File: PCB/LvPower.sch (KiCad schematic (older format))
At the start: 0 parts

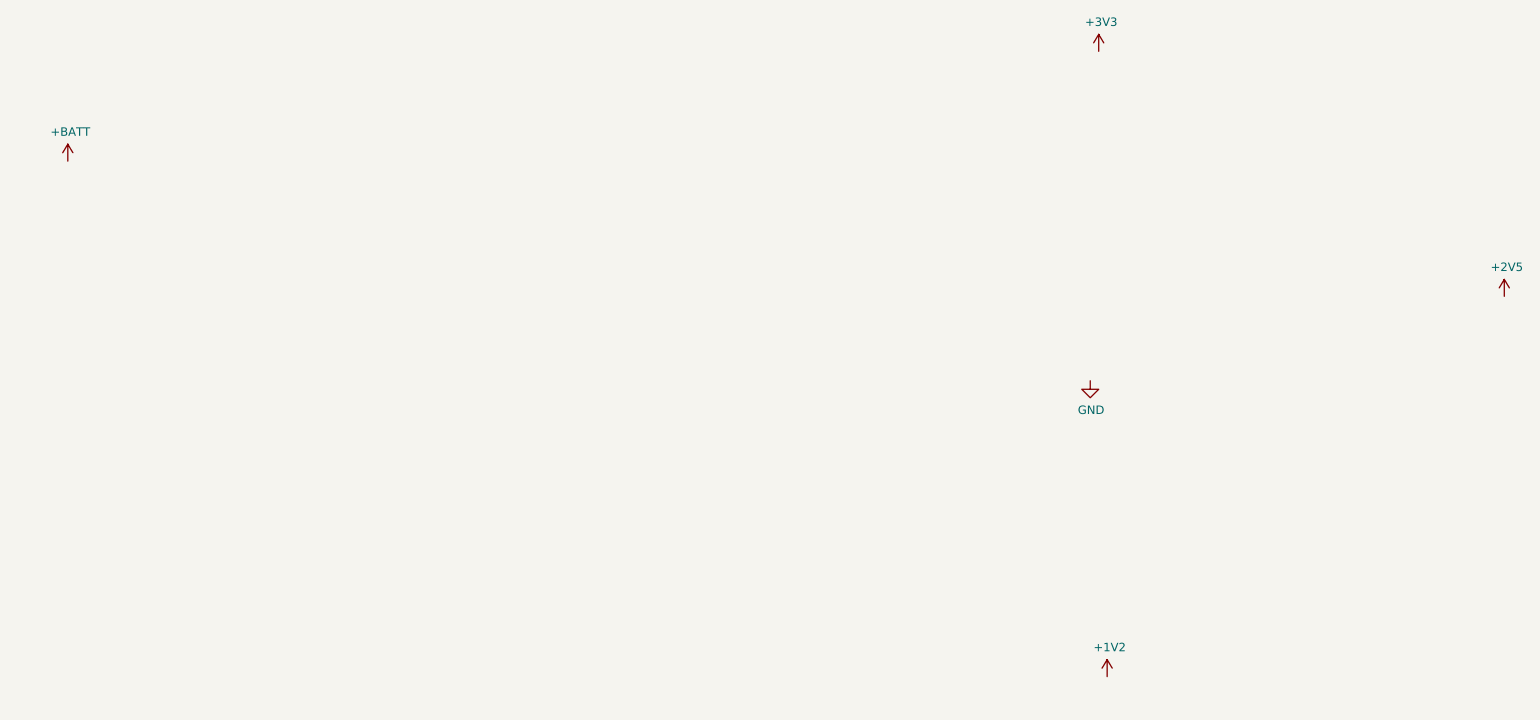
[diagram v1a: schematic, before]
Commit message: Cleanup FPGA ground pins in library, begin adding components to schematic
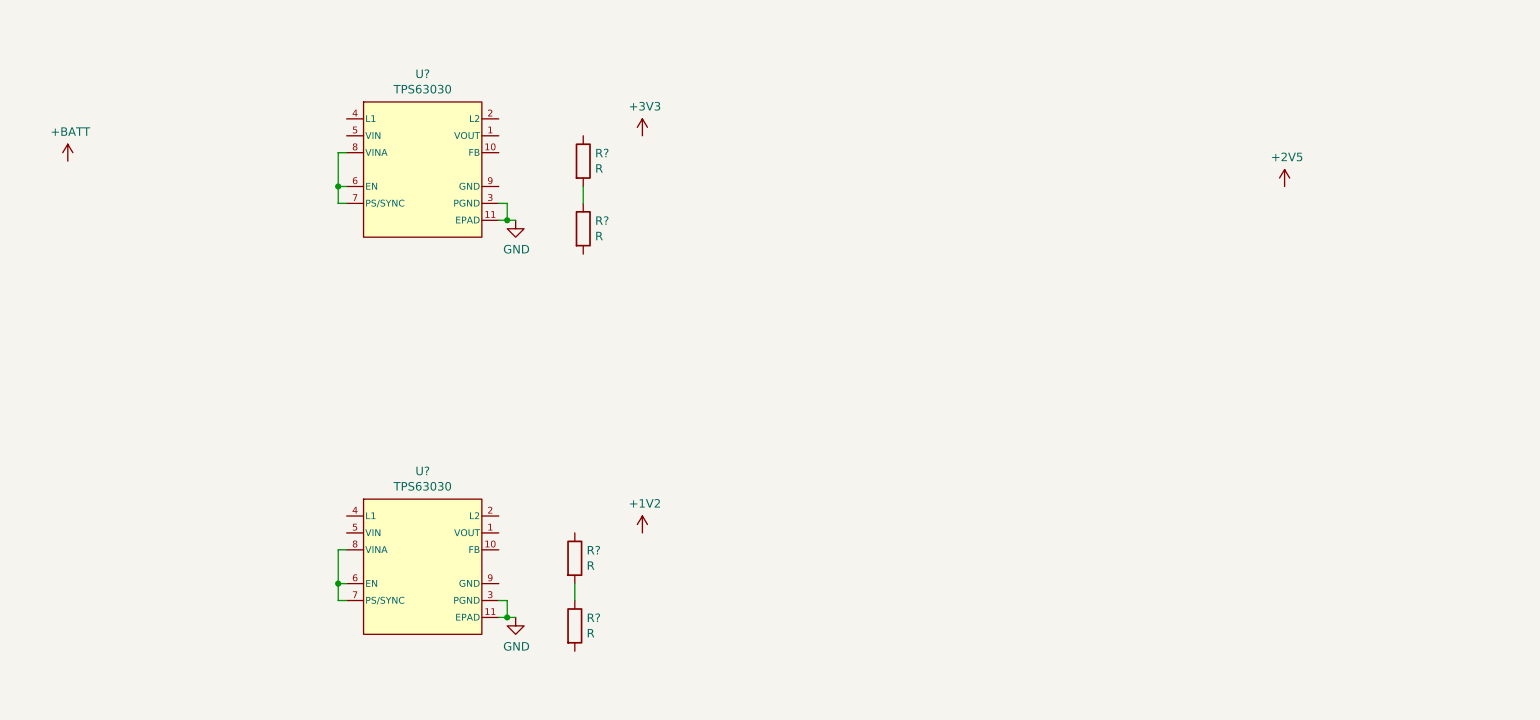
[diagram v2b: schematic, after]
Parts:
- added R? (x4): R, symbol Device:R
- added U? (x2): TPS63030, Parts:WSON10-PAD, symbol Parts:TPS63030
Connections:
- net GND: now also U?.11 (EPAD), U?.11 (EPAD), U?.3 (PGND), U?.3 (PGND)
- new net: U?.6 (EN), U?.7 (PS/SYNC), U?.8 (VINA) (x2)
- new net: R?.1, R?.2 (x2)
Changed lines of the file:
@@
 L power:+3V3 #PWR?
 U 1 1 5DCD8EE2
-P 8050 2000
-F 0 "#PWR?" H 8050 1850 50  0001 C CNN
-F 1 "+3V3" H 8065 2173 50  0000 C CNN
-F 2 "" H 8050 2000 50  0001 C CNN
-F 3 "" H 8050 2000 50  0001 C CNN
-	1    8050 2000
+P 5350 2500
+F 0 "#PWR?" H 5350 2350 50  0001 C CNN
+F 1 "+3V3" H 5365 2673 50  0000 C CNN
+F 2 "" H 5350 2500 50  0001 C CNN
+F 3 "" H 5350 2500 50  0001 C CNN
+	1    5350 2500
 	1    0    0    -1
 $EndComp
@@
 L power:+1V2 #PWR?
 U 1 1 5DCD9F72
-P 8100 5700
-F 0 "#PWR?" H 8100 5550 50  0001 C CNN
-F 1 "+1V2" H 8115 5873 50  0000 C CNN
-F 2 "" H 8100 5700 50  0001 C CNN
-F 3 "" H 8100 5700 50  0001 C CNN
-	1    8100 5700
+P 5350 4850
+F 0 "#PWR?" H 5350 4700 50  0001 C CNN
+F 1 "+1V2" H 5365 5023 50  0000 C CNN
+F 2 "" H 5350 4850 50  0001 C CNN
+F 3 "" H 5350 4850 50  0001 C CNN
+	1    5350 4850
 	1    0    0    -1
 $EndComp
@@
 L power:+2V5 #PWR?
 U 1 1 5DCDA97B
-P 10450 3450
-F 0 "#PWR?" H 10450 3300 50  0001 C CNN
-F 1 "+2V5" H 10465 3623 50  0000 C CNN
-F 2 "" H 10450 3450 50  0001 C CNN
-F 3 "" H 10450 3450 50  0001 C CNN
-	1    10450 3450
+P 9150 2800
+F 0 "#PWR?" H 9150 2650 50  0001 C CNN
+F 1 "+2V5" H 9165 2973 50  0000 C CNN
+F 2 "" H 9150 2800 50  0001 C CNN
+F 3 "" H 9150 2800 50  0001 C CNN
+	1    9150 2800
 	1    0    0    -1
 $EndComp
@@
 L power:GND #PWR?
 U 1 1 5DCDBC9C
-P 8000 3950
-F 0 "#PWR?" H 8000 3700 50  0001 C CNN
-F 1 "GND" H 8005 3777 50  0000 C CNN
-F 2 "" H 8000 3950 50  0001 C CNN
-F 3 "" H 8000 3950 50  0001 C CNN
-	1    8000 3950
+P 4600 3000
+F 0 "#PWR?" H 4600 2750 50  0001 C CNN
+F 1 "GND" H 4605 2827 50  0000 C CNN
+F 2 "" H 4600 3000 50  0001 C CNN
+F 3 "" H 4600 3000 50  0001 C CNN
+	1    4600 3000
 	1    0    0    -1
 $EndComp
+$Comp
+L Parts:TPS63030 U?
+U 1 1 5DCF7F00
+P 4050 2700
+F 0 "U?" H 4050 3265 50  0000 C CNN
+F 1 "TPS63030" H 4050 3174 50  0000 C CNN
+F 2 "Parts:WSON10-PAD" H 4050 2250 60  0001 C CNN
+F 3 "http://www.ti.com/product/TPS63030" H 3600 2600 60  0001 C CNN
+	1    4050 2700
+	1    0    0    -1
+$EndComp
+$Comp
+L Parts:TPS63030 U?
+U 1 1 5DCF8885
+P 4050 5050
+F 0 "U?" H 4050 5615 50  0000 C CNN
+F 1 "TPS63030" H 4050 5524 50  0000 C CNN
+F 2 "Parts:WSON10-PAD" H 4050 4600 60  0001 C CNN
+F 3 "http://www.ti.com/product/TPS63030" H 3600 4950 60  0001 C CNN
+	1    4050 5050
+	1    0    0    -1
+$EndComp
+$Comp
+L power:GND #PWR?
+U 1 1 5DCF9CED
+P 4600 5350
+F 0 "#PWR?" H 4600 5100 50  0001 C CNN
+F 1 "GND" H 4605 5177 50  0000 C CNN
+F 2 "" H 4600 5350 50  0001 C CNN
+F 3 "" H 4600 5350 50  0001 C CNN
+	1    4600 5350
+	1    0    0    -1
+$EndComp
+Wire Wire Line
+	4600 5350 4550 5350
+Wire Wire Line
+	4500 3000 4550 3000
+Wire Wire Line
+	4500 2900 4550 2900
+Wire Wire Line
+	4550 2900 4550 3000
+Connection ~ 4550 3000
+Wire Wire Line
+	4550 3000 4600 3000
+Wire Wire Line
+	4500 5250 4550 5250
+Wire Wire Line
+	4550 5250 4550 5350
+Connection ~ 4550 5350
+Wire Wire Line
+	4550 5350 4500 5350
+$Comp
+L Device:R R?
+U 1 1 5DCFD0C2
+P 5000 3050
+F 0 "R?" H 5070 3096 50  0000 L CNN
+F 1 "R" H 5070 3005 50  0000 L CNN
+F 2 "" V 4930 3050 50  0001 C CNN
+F 3 "~" H 5000 3050 50  0001 C CNN
+	1    5000 3050
+	1    0    0    -1
+$EndComp
+$Comp
+L Device:R R?
+U 1 1 5DCFE76B
+P 5000 2650
+F 0 "R?" H 5070 2696 50  0000 L CNN
+F 1 "R" H 5070 2605 50  0000 L CNN
+F 2 "" V 4930 2650 50  0001 C CNN
+F 3 "~" H 5000 2650 50  0001 C CNN
+	1    5000 2650
+	1    0    0    -1
+$EndComp
+Wire Wire Line
+	5000 2800 5000 2900
+$Comp
+L Device:R R?
+U 1 1 5DD00F6F
+P 4950 5000
+F 0 "R?" H 5020 5046 50  0000 L CNN
+F 1 "R" H 5020 4955 50  0000 L CNN
+F 2 "" V 4880 5000 50  0001 C CNN
+F 3 "~" H 4950 5000 50  0001 C CNN
+	1    4950 5000
+	1    0    0    -1
+$EndComp
+$Comp
+L Device:R R?
+U 1 1 5DD0194C
+P 4950 5400
+F 0 "R?" H 5020 5446 50  0000 L CNN
+F 1 "R" H 5020 5355 50  0000 L CNN
+F 2 "" V 4880 5400 50  0001 C CNN
+F 3 "~" H 4950 5400 50  0001 C CNN
+	1    4950 5400
+	1    0    0    -1
+$EndComp
+Wire Wire Line
+	4950 5150 4950 5250
+Wire Wire Line
+	3600 2600 3550 2600
+Wire Wire Line
+	3550 2600 3550 2800
+Wire Wire Line
+	3550 2800 3600 2800
+Wire Wire Line
+	3550 2800 3550 2900
+Wire Wire Line
+	3550 2900 3600 2900
+Connection ~ 3550 2800
+Wire Wire Line
+	3600 4950 3550 4950
+Wire Wire Line
+	3550 4950 3550 5150
+Wire Wire Line
+	3550 5150 3600 5150
+Wire Wire Line
+	3550 5150 3550 5250
+Wire Wire Line
+	3550 5250 3600 5250
+Connection ~ 3550 5150
 $EndSCHEMATC

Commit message: Add linear regulator and JST-PH connector to library
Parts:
- added R? (x2): R, symbol Device:R
- added U?: AP2202K-ADJTRG1, Parts:SOT23-5, symbol Parts:AP2202K-ADJTRG1
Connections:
- wire segments 20 -> 21
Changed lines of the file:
@@
 L power:+2V5 #PWR?
 U 1 1 5DCDA97B
-P 9150 2800
-F 0 "#PWR?" H 9150 2650 50  0001 C CNN
-F 1 "+2V5" H 9165 2973 50  0000 C CNN
-F 2 "" H 9150 2800 50  0001 C CNN
-F 3 "" H 9150 2800 50  0001 C CNN
-	1    9150 2800
+P 9250 2800
+F 0 "#PWR?" H 9250 2650 50  0001 C CNN
+F 1 "+2V5" H 9265 2973 50  0000 C CNN
+F 2 "" H 9250 2800 50  0001 C CNN
+F 3 "" H 9250 2800 50  0001 C CNN
+	1    9250 2800
 	1    0    0    -1
 $EndComp
@@
 L power:+BATT #PWR?
 U 1 1 5DCDADE4
-P 1950 2650
-F 0 "#PWR?" H 1950 2500 50  0001 C CNN
-F 1 "+BATT" H 1965 2823 50  0000 C CNN
-F 2 "" H 1950 2650 50  0001 C CNN
-F 3 "" H 1950 2650 50  0001 C CNN
-	1    1950 2650
+P 1750 2100
+F 0 "#PWR?" H 1750 1950 50  0001 C CNN
+F 1 "+BATT" H 1765 2273 50  0000 C CNN
+F 2 "" H 1750 2100 50  0001 C CNN
+F 3 "" H 1750 2100 50  0001 C CNN
+	1    1750 2100
 	1    0    0    -1
 $EndComp
@@
 	3550 5250 3600 5250
 Connection ~ 3550 5150
+$Comp
+L Device:R R?
+U 1 1 5DCE675A
+P 8950 2950
+F 0 "R?" H 9020 2996 50  0000 L CNN
+F 1 "R" H 9020 2905 50  0000 L CNN
+F 2 "" V 8880 2950 50  0001 C CNN
+F 3 "~" H 8950 2950 50  0001 C CNN
+	1    8950 2950
+	1    0    0    -1
+$EndComp
+$Comp
+L Device:R R?
+U 1 1 5DCE7121
+P 8950 3350
+F 0 "R?" H 9020 3396 50  0000 L CNN
+F 1 "R" H 9020 3305 50  0000 L CNN
+F 2 "" V 8880 3350 50  0001 C CNN
+F 3 "~" H 8950 3350 50  0001 C CNN
+	1    8950 3350
+	1    0    0    -1
+$EndComp
+Wire Wire Line
+	8950 3100 8950 3200
+$Comp
+L Parts:AP2202K-ADJTRG1 U?
+U 1 1 5DCE8C9B
+P 8200 2900
+F 0 "U?" H 8200 3265 50  0000 C CNN
+F 1 "AP2202K-ADJTRG1" H 8200 3174 50  0000 C CNN
+F 2 "Parts:SOT23-5" H 8200 2550 50  0001 C CNN
+F 3 "https://www.diodes.com/part/view/AP2202" H 8200 2550 50  0001 C CNN
+	1    8200 2900
+	1    0    0    -1
+$EndComp
 $EndSCHEMATC

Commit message: Switch to cheaper linear regulator (with better datasheet), finish LvPower schematic
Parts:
- removed R? (x4): R, symbol Device:R
- removed U?: AP2202K-ADJTRG1, Parts:SOT23-5, symbol Parts:AP2202K-ADJTRG1
- removed U?: TPS63030, Parts:WSON10-PAD, symbol Parts:TPS63030
- added C? (x6): 10uF, Capacitors_SMD:C_0805_HandSoldering, symbol Device:C_Small
- added C? (x2): 100nF, Capacitors_SMD:C_0402, symbol Device:C_Small
- added C? (x2): 1uF, Capacitors_SMD:C_0603_HandSoldering, symbol Device:C_Small
- added L? (x2): 1.5uH, Inductors:Inductor_Taiyo-Yuden_MD-3030, symbol Device:L_Core_Ferrite_Small
- added NT? (x2): Net-Tie_2, symbol Device:Net-Tie_2
- added R?: 280k, Resistors_SMD:R_0603_HandSoldering, symbol Device:R
- added R?: 200k, Resistors_SMD:R_0603_HandSoldering, symbol Device:R
- added R?: 120k, Resistors_SMD:R_0805_HandSoldering, symbol Device:R
- added U?: TPS63030, Parts:WSON10-PAD, symbol Parts:TPS63030
- added U?: TCR2EF25, Parts:SOT23-5, symbol Parts:TCR2EF25
- R?: value R -> 200k; footprint (none) -> Resistors_SMD:R_0603_HandSoldering
- R?: value R -> 1M; footprint (none) -> Resistors_SMD:R_0805_HandSoldering
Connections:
- net labels added: GNDA-1V2, GNDA-3V3
- wire segments 21 -> 96
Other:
- moved on the sheet: R?

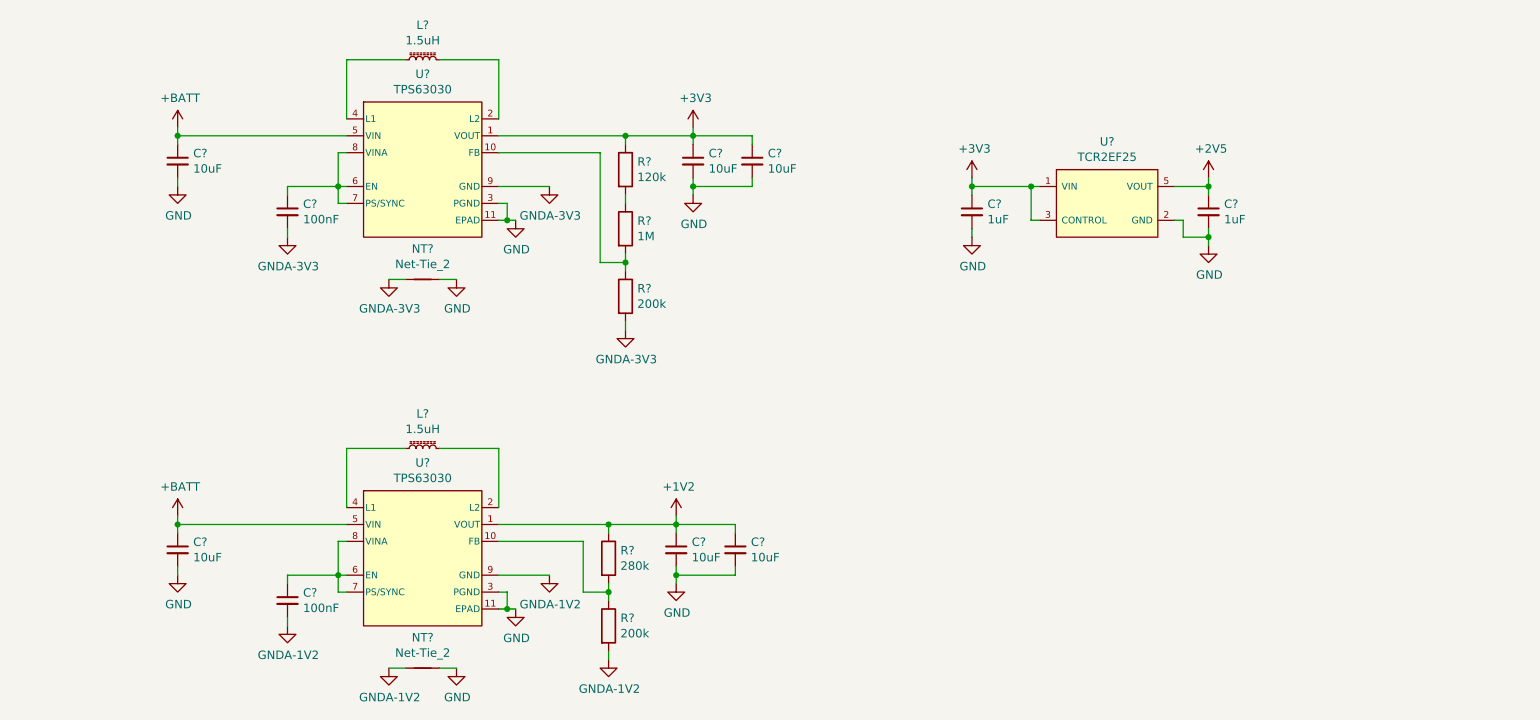
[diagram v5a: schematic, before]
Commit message: Switch 1.2V supply to use new buck regulator
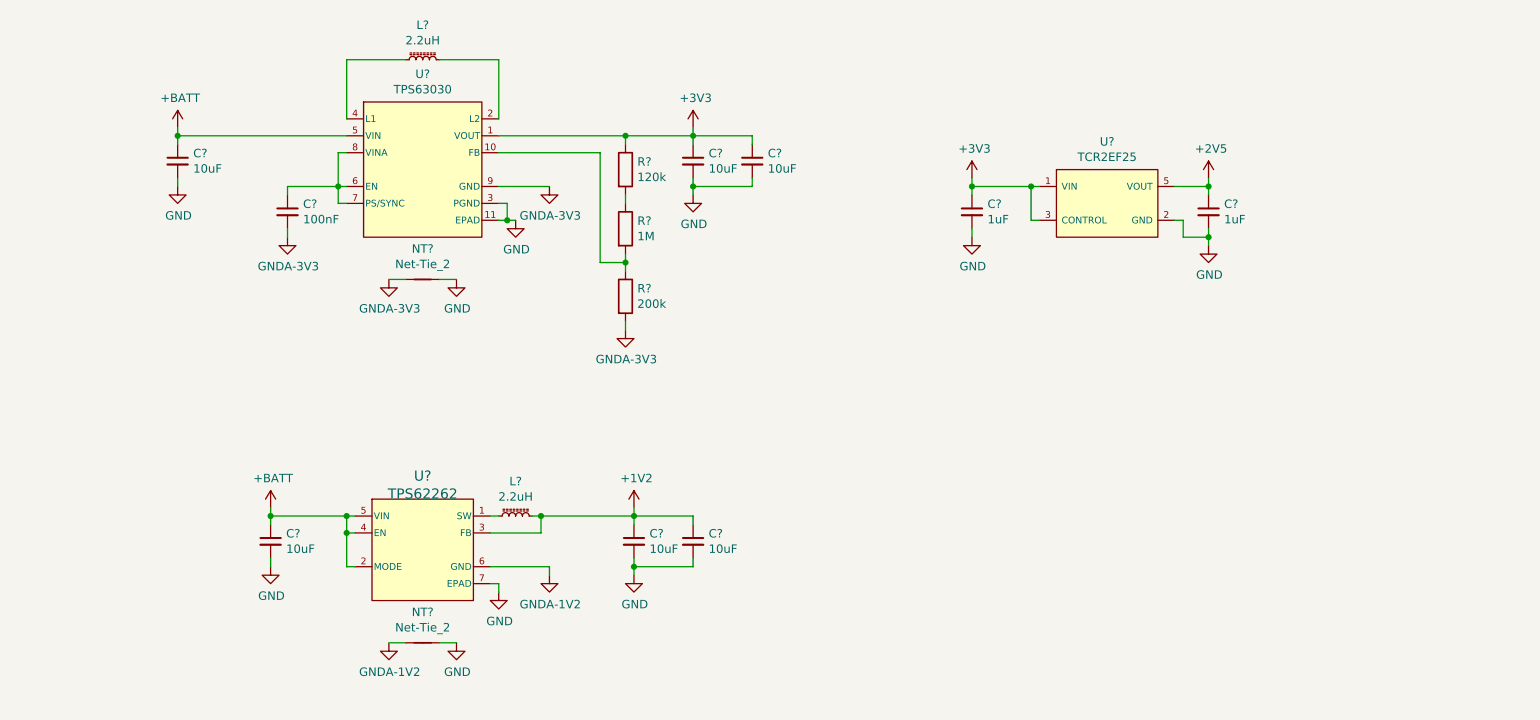
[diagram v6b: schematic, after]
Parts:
- removed C?: 100nF, Capacitors_SMD:C_0402, symbol Device:C_Small
- removed L?: 1.5uH, Inductors:Inductor_Taiyo-Yuden_MD-3030, symbol Device:L_Core_Ferrite_Small
- removed R?: 280k, Resistors_SMD:R_0603_HandSoldering, symbol Device:R
- removed R?: 200k, Resistors_SMD:R_0603_HandSoldering, symbol Device:R
- removed U?: TPS63030, Parts:WSON10-PAD, symbol Parts:TPS63030
- added L?: 2.2uH, Inductors:Inductor_Taiyo-Yuden_MD-3030, symbol Device:L_Core_Ferrite_Small
- added U?: TPS62262, Parts:WSON6-PAD, symbol Parts:TPS62262
- L?: value 1.5uH -> 2.2uH
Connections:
- net +1V2: now also L?.2, U?.3 (FB)
- net +BATT: now also U?.2 (MODE), U?.4 (EN), U?.5 (VIN)
- net GND: now also U?.7 (EPAD)
- net GNDA-1V2: now also U?.6 (GND)
- net at U?.2 (L2): now also L?.2
- net at U?.4 (L1): now also L?.1
- new net: L?.1, U?.1 (SW)
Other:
- moved on the sheet: C?, L?, NT?
